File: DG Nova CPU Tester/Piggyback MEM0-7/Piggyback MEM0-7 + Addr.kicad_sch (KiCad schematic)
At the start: 26 parts, among them J1 Conn_02x18_Odd_Even, J22 Arduino Digital Pins, J23 Arduino Digital Pins, J3 Conn_01x17, J5 Conn_01x08, J6 Conn_01x08, SW1 Arduino Mega Reset, SW4 SW_DIP_x04, U1 74LS03, U2 74LS03, U3 74LS04, U4 74HC595, U5 74LS03, U6 74LS03, U7 74LS03, U8 74LS03, U9 74HC595

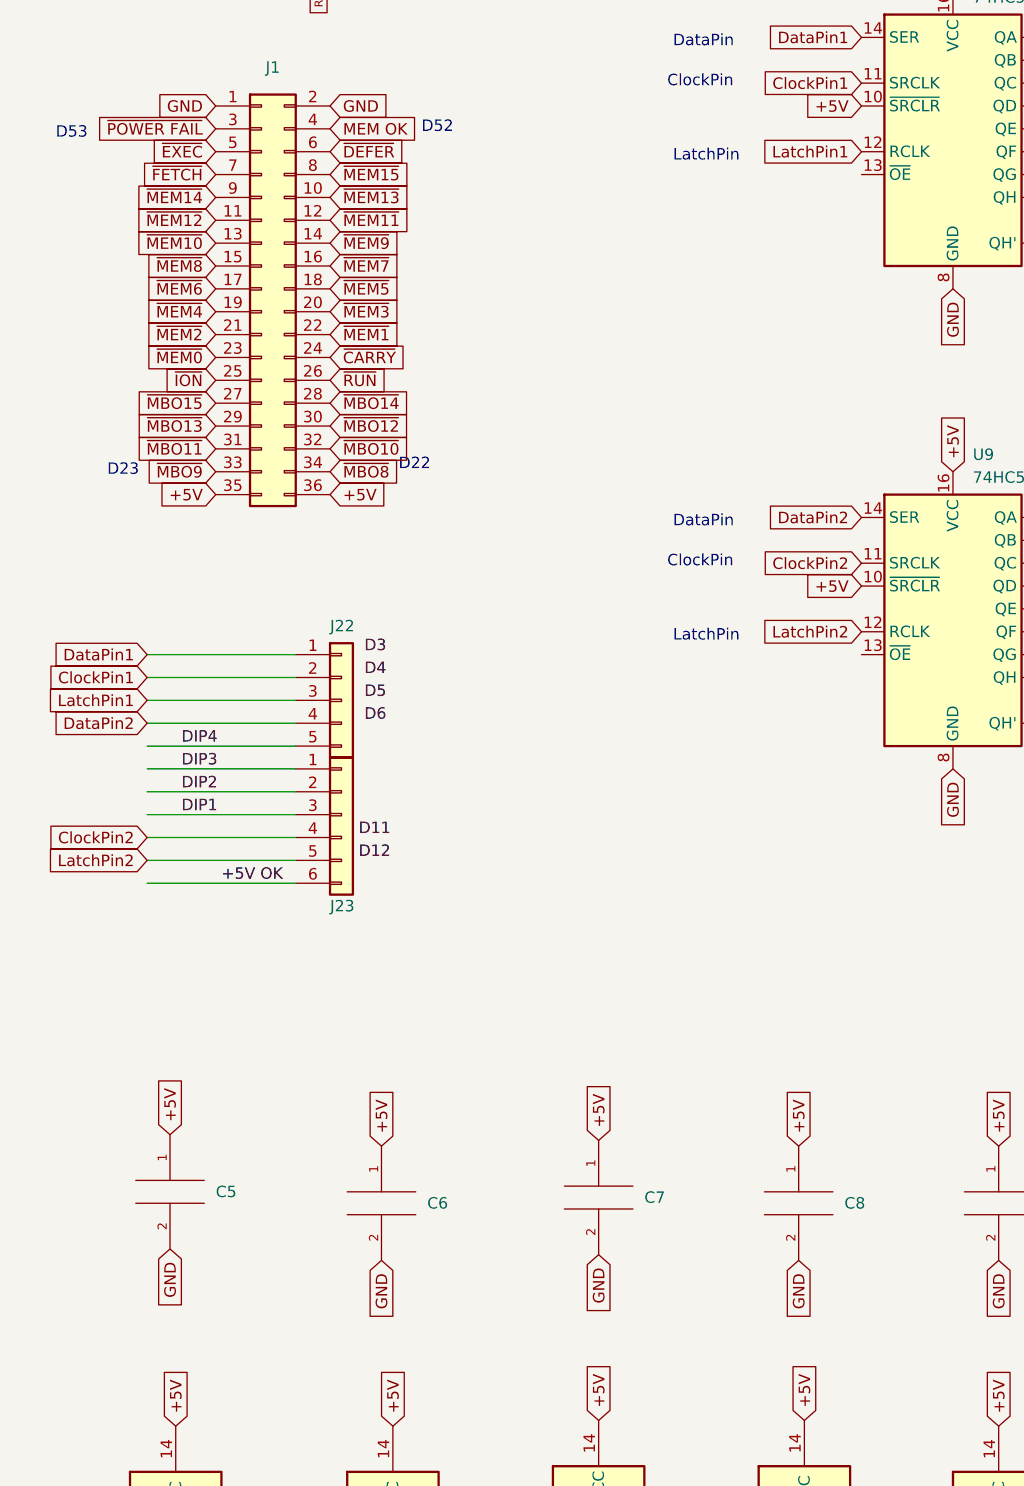
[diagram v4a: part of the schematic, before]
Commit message: fix /CE to GND
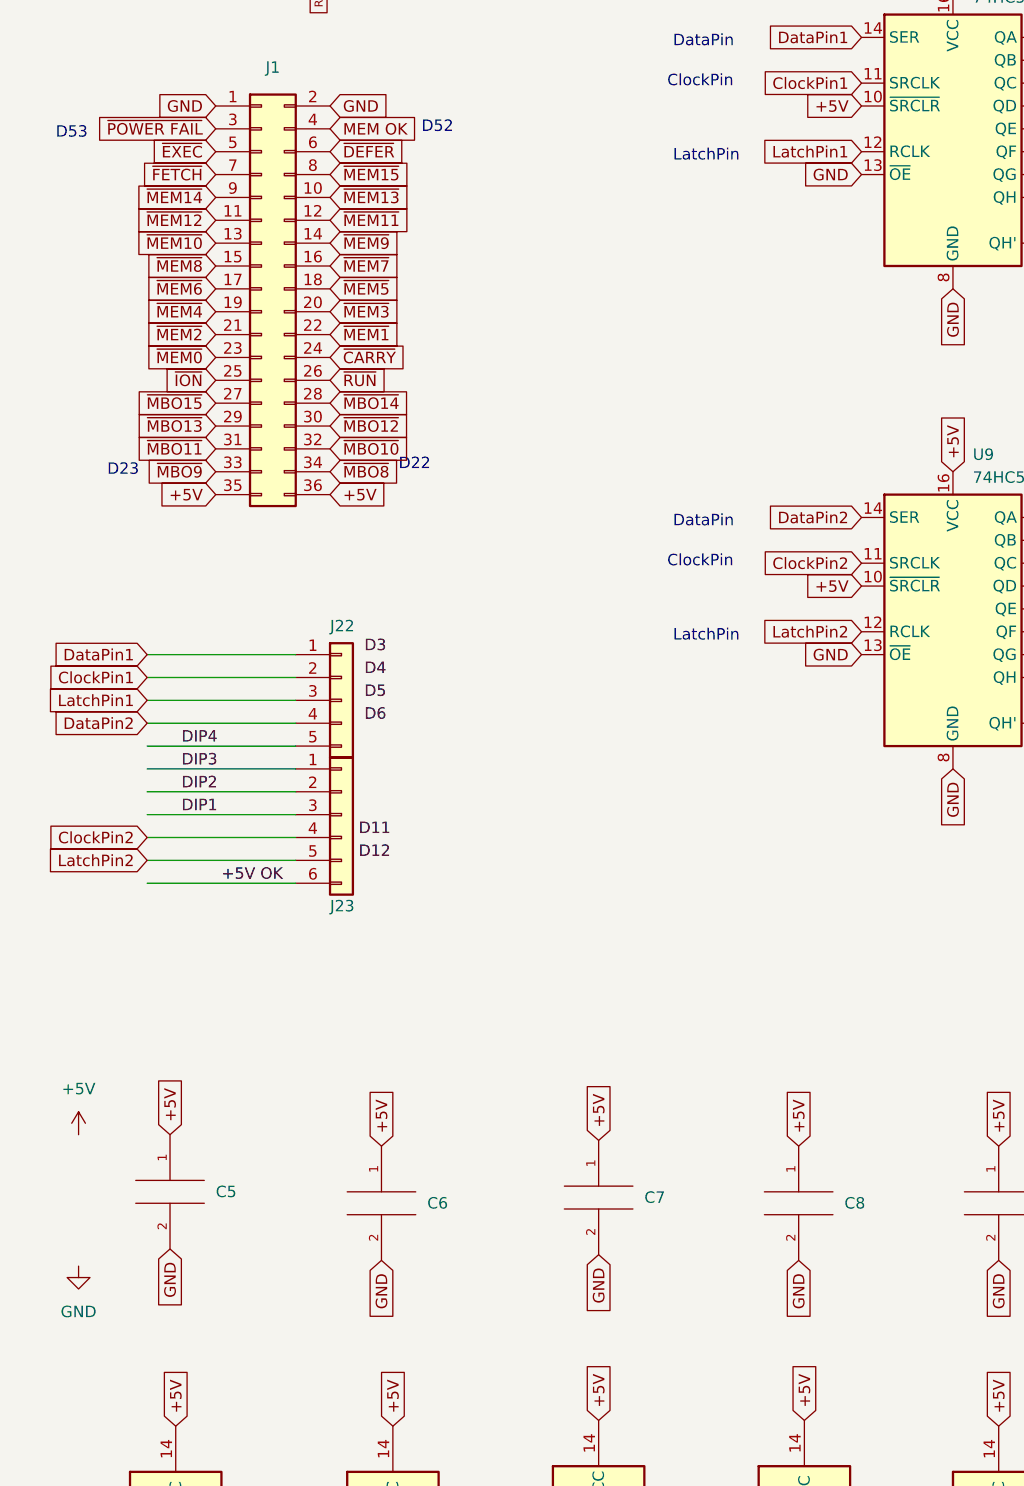
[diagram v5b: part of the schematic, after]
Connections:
- net GND: now also U4.13 (~{OE}), U9.13 (~{OE})
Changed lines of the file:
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@@
+    )
+  )
+  (global_label "GND" (shape input) (at 107.315 59.055 180) (fields_autoplaced)
+    (effects (font (size 1.27 1.27)) (justify right))
+    (property "Intersheetrefs" "${INTERSHEET_REFS}" (at 100.4593 59.055 0)
+      (effects (font (size 1.27 1.27)) (justify right) hide)
     )
   )
@@
     )
   )
+  (global_label "GND" (shape input) (at 107.315 112.395 180) (fields_autoplaced)
+    (effects (font (size 1.27 1.27)) (justify right))
+    (property "Intersheetrefs" "${INTERSHEET_REFS}" (at 100.4593 112.395 0)
+      (effects (font (size 1.27 1.27)) (justify right) hide)
+    )
+  )
   (global_label "GND" (shape input) (at 100.33 179.705 270) (fields_autoplaced)
     (effects (font (size 1.27 1.27)) (justify right))
@@
         (path "/fe0be92e-1d85-43cc-bb82-88d36766eebc"
           (reference "C2") (unit 1)
+        )
+      )
+    )
+  )
+  (symbol (lib_id "power:+5V") (at 20.32 165.735 0) (unit 1)
+    (in_bom yes) (on_board yes) (dnp no) (fields_autoplaced)
+    (property "Reference" "#PWR01" (at 20.32 169.545 0)
+      (effects (font (size 1.27 1.27)) hide)
+    )
+    (property "Value" "+5V" (at 20.32 160.655 0)
+      (effects (font (size 1.27 1.27)))
+    )
+    (property "Footprint" "" (at 20.32 165.735 0)
+      (effects (font (size 1.27 1.27)) hide)
+    )
+    (property "Datasheet" "" (at 20.32 165.735 0)
+      (effects (font (size 1.27 1.27)) hide)
+    )
+    (pin "1")
+    (instances
+      (project "Piggyback MEM0-7 + Addr"
+        (path "/fe0be92e-1d85-43cc-bb82-88d36766eebc"
+          (reference "#PWR01") (unit 1)
         )
       )
@@
         )
       )
+    )
+  )
+  (symbol (lib_id "power:GND") (at 20.32 180.34 0) (unit 1)
+    (in_bom yes) (on_board yes) (dnp no) (fields_autoplaced)
+    (property "Reference" "#PWR02" (at 20.32 186.69 0)
+      (effects (font (size 1.27 1.27)) hide)
+    )
+    (property "Value" "GND" (at 20.32 185.42 0)
+      (effects (font (size 1.27 1.27)))
+    )
+    (property "Footprint" "" (at 20.32 180.34 0)
+      (effects (font (size 1.27 1.27)) hide)
+    )
+    (property "Datasheet" "" (at 20.32 180.34 0)
+      (effects (font (size 1.27 1.27)) hide)
+    )
+    (pin "1")
+    (instances
+      (project "Piggyback MEM0-7 + Addr"
+        (path "/fe0be92e-1d85-43cc-bb82-88d36766eebc"
+          (reference "#PWR02") (unit 1)
+        )
+      )

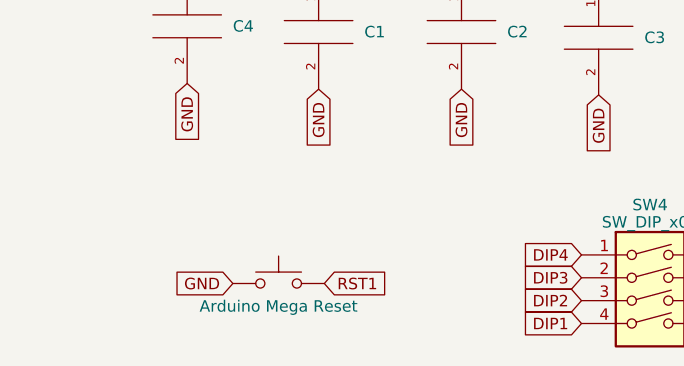
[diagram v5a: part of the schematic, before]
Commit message: Fix reset button polarity
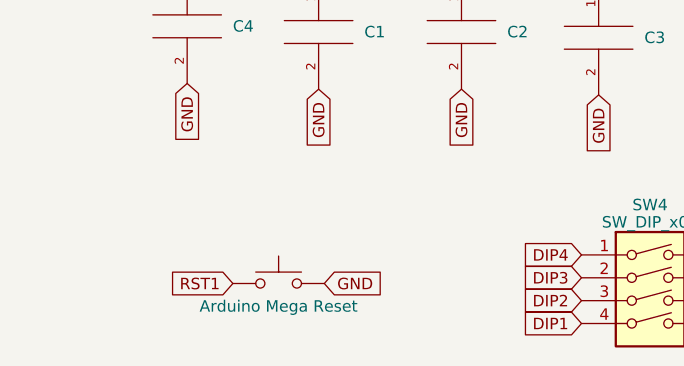
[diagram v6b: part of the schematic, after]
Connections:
- net GND: now also SW1.2; no longer SW1.1
- net RST1: now also SW1.1; no longer SW1.2

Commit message: x
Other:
- note added: "Address/Data Switches Set"
- note added: "Switch Command Code"
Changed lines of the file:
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@@
     (stroke (width 0) (type default))
+  )
+  (rectangle (start 208.28 20.955) (end 254.635 310.515)
+    (stroke (width 0) (type default))
+    (fill (type none))
+  )
+  (rectangle (start 151.765 19.05) (end 195.58 174.625)
+    (stroke (width 0) (type default))
+    (fill (type none))
   )
   (text "D52" (at 58.42 54.61 0)
@@
     (effects (font (size 1.27 1.27)) (justify left bottom))
   )
+  (text "Switch Command Code" (at 164.465 16.51 0)
+    (effects (font (size 1.27 1.27) (thickness 0.254) bold) (justify left bottom))
+  )
+  (text "Address/Data Switches Set" (at 219.71 17.78 0)
+    (effects (font (size 1.27 1.27) (thickness 0.254) bold) (justify left bottom))
+  )
   (text "ClockPin" (at 85.725 102.87 0)
